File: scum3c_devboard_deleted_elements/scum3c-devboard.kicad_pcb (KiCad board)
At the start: 4 copper layers, 30 x 30 mm, 23 parts, among them J1 Conn_01x14, U8 scum3, U9AB1 MPU-9250

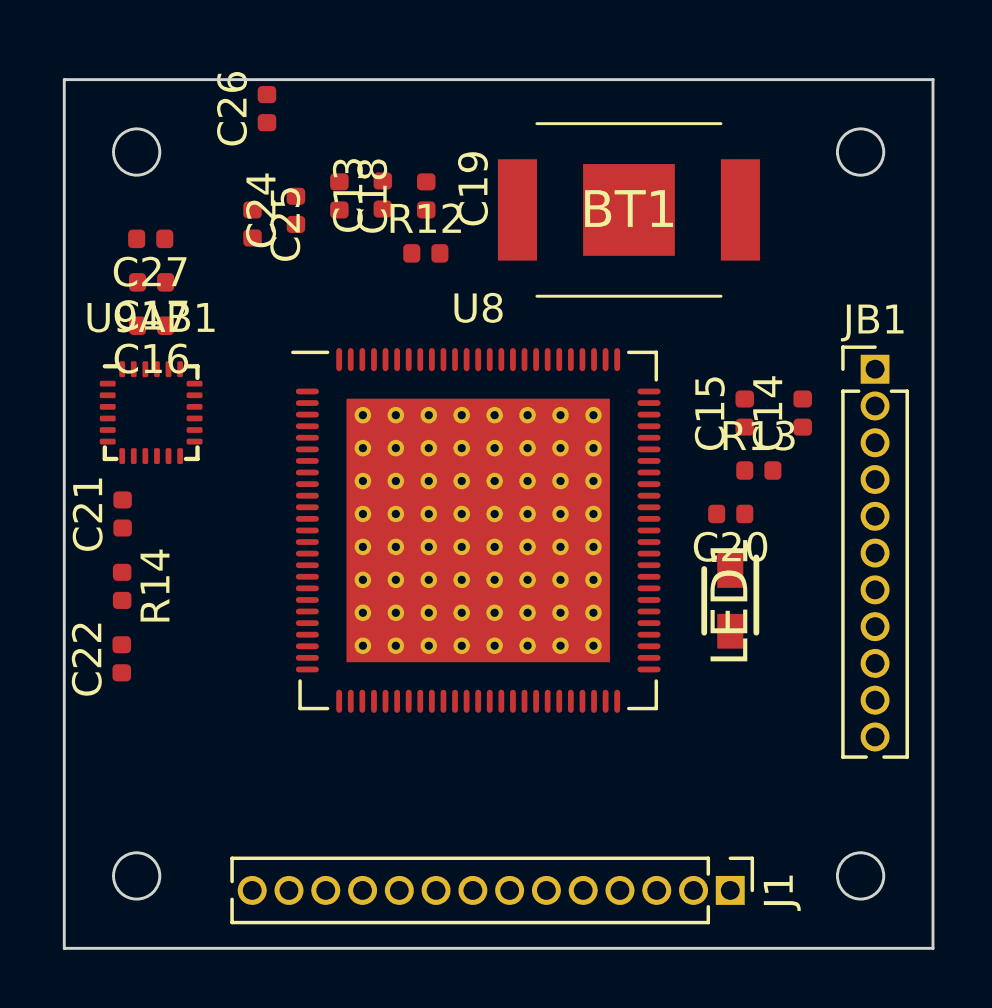
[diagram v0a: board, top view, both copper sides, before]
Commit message: Revert "added gpio8-10"
This reverts commit daf7284f57cd8196d10e3621e3573955ecb68719.
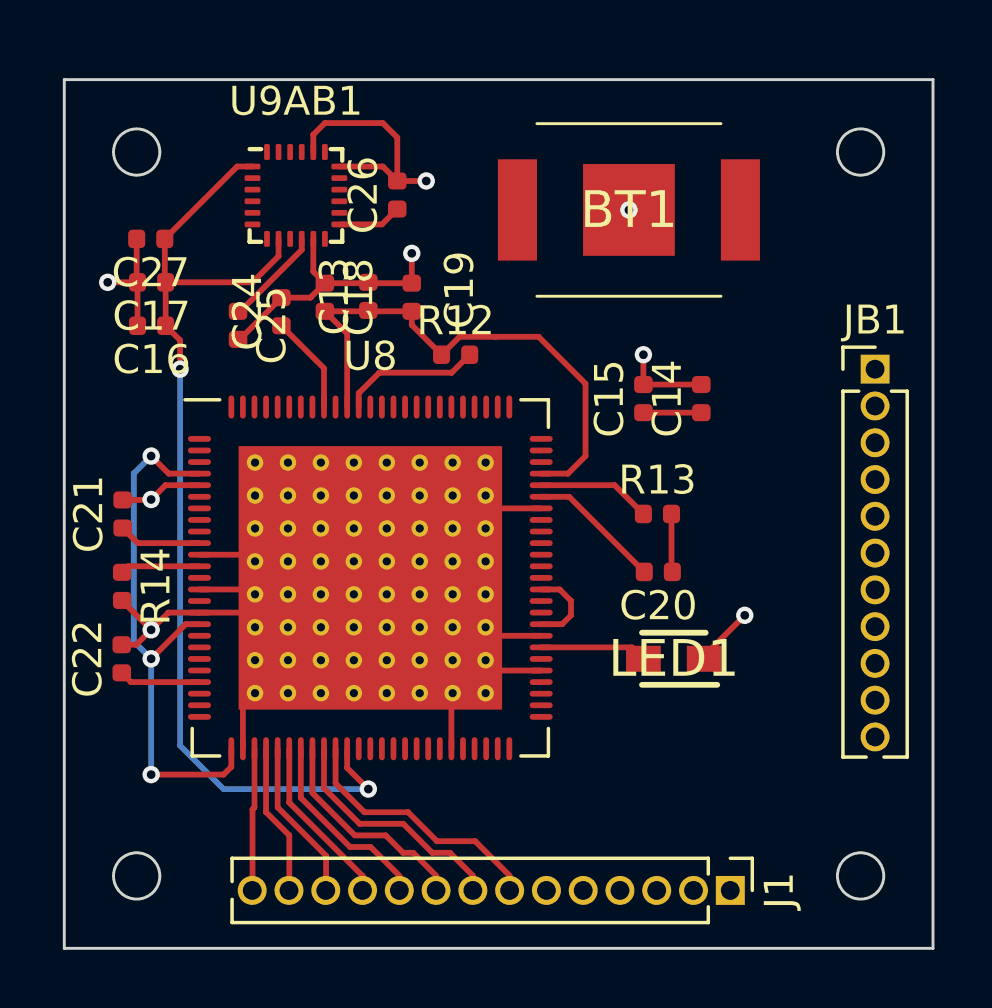
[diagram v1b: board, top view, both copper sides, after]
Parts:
- moved U9AB1 9.01 mm to (95.5, 81.5)
- moved C26 5.40 mm to (99.0, 81.5)
- moved U8 4.07 mm to (98.1, 94.7)
- moved R13 3.81 mm to (108.0, 92.5)
- moved R12 3.65 mm to (101.0, 87.0)
- moved C13 3.54 mm to (98.0, 85.0)
- moved C14 3.54 mm to (109.5, 88.5)
- moved C15 3.54 mm to (107.5, 88.5)
- moved C18 3.54 mm to (96.5, 85.0)
- moved C19 3.54 mm to (99.5, 85.0)
- moved C24 3.54 mm to (95.0, 85.5)
- moved C25 3.54 mm to (93.5, 86.0)
- moved C20 3.20 mm to (108.0, 94.5)
- moved LED1 2.79 mm to (108.5, 97.5), turned to 180 degrees
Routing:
- net GND: track 0.00 -> 53.1 mm, vias 0 -> 8
- net +VDDIO: track 0.00 -> 35.5 mm, vias 0 -> 2
- net +VBAT: track 0.00 -> 23.9 mm, vias 0 -> 3
- net +VDDD: track 0.00 -> 18.8 mm
- net /GPIO7: track 0.00 -> 8.54 mm
- net /GPIO6: track 0.00 -> 7.77 mm
- net /GPIO5: track 0.00 -> 7.00 mm
- net /GPIO4: track 0.00 -> 6.22 mm
- net /GPIO3: track 0.00 -> 5.45 mm
- net /GPIO2: track 0.00 -> 5.09 mm
- net Net-(R12-Pad2): track 0.00 -> 4.86 mm
- net /GPIO1: track 0.00 -> 4.73 mm
- net /scumsheet/AUX_LDO_OUTPUT: track 0.00 -> 4.64 mm
- net /GPIO0: track 0.00 -> 4.42 mm
- net Net-(R13-Pad1): track 0.00 -> 3.94 mm
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
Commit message: deleted tracks
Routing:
- net GND: track 53.1 -> 0.00 mm, vias 8 -> 0
- net +VDDIO: track 35.5 -> 0.00 mm, vias 2 -> 0
- net +VBAT: track 23.9 -> 0.00 mm, vias 3 -> 0
- net +VDDD: track 18.8 -> 0.00 mm
- net /GPIO7: track 8.54 -> 0.00 mm
- net /GPIO6: track 7.77 -> 0.00 mm
- net /GPIO5: track 7.00 -> 0.00 mm
- net /GPIO4: track 6.22 -> 0.00 mm
- net /GPIO3: track 5.45 -> 0.00 mm
- net /GPIO2: track 5.09 -> 0.00 mm
- net Net-(R12-Pad2): track 4.86 -> 0.00 mm
- net /GPIO1: track 4.73 -> 0.00 mm
- net /scumsheet/AUX_LDO_OUTPUT: track 4.64 -> 0.00 mm
- net /GPIO0: track 4.42 -> 0.00 mm
- net Net-(R13-Pad1): track 3.94 -> 0.00 mm
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
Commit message: placed components
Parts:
- moved C26 13.9 mm to (90.5, 92.5), turned to 180 degrees
- moved C15 8.60 mm to (114.5, 83.5), turned to 0 degrees
- moved C27 8.30 mm to (98.0, 79.5), turned to 90 degrees
- moved C16 7.88 mm to (95.0, 79.5), turned to 90 degrees
- moved C17 7.79 mm to (96.5, 79.5), turned to 90 degrees
- moved U9AB1 6.52 mm to (92.0, 87.0), turned to 270 degrees
- moved C14 5.83 mm to (114.5, 85.5), turned to 0 degrees
- moved R13 5.71 mm to (111.5, 88.0)
- moved C20 5.70 mm to (111.5, 90.0)
- moved C25 5.43 mm to (90.5, 90.5), turned to 0 degrees
- moved U8 4.61 mm to (102.4, 93.2)
- moved LED1 4.54 mm to (111.5, 94.0), turned to 270 degrees
- moved R12 3.65 mm to (100.0, 83.5)
- moved C24 3.23 mm to (93.0, 83.0)
- moved C13 2.50 mm to (96.5, 83.0)
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
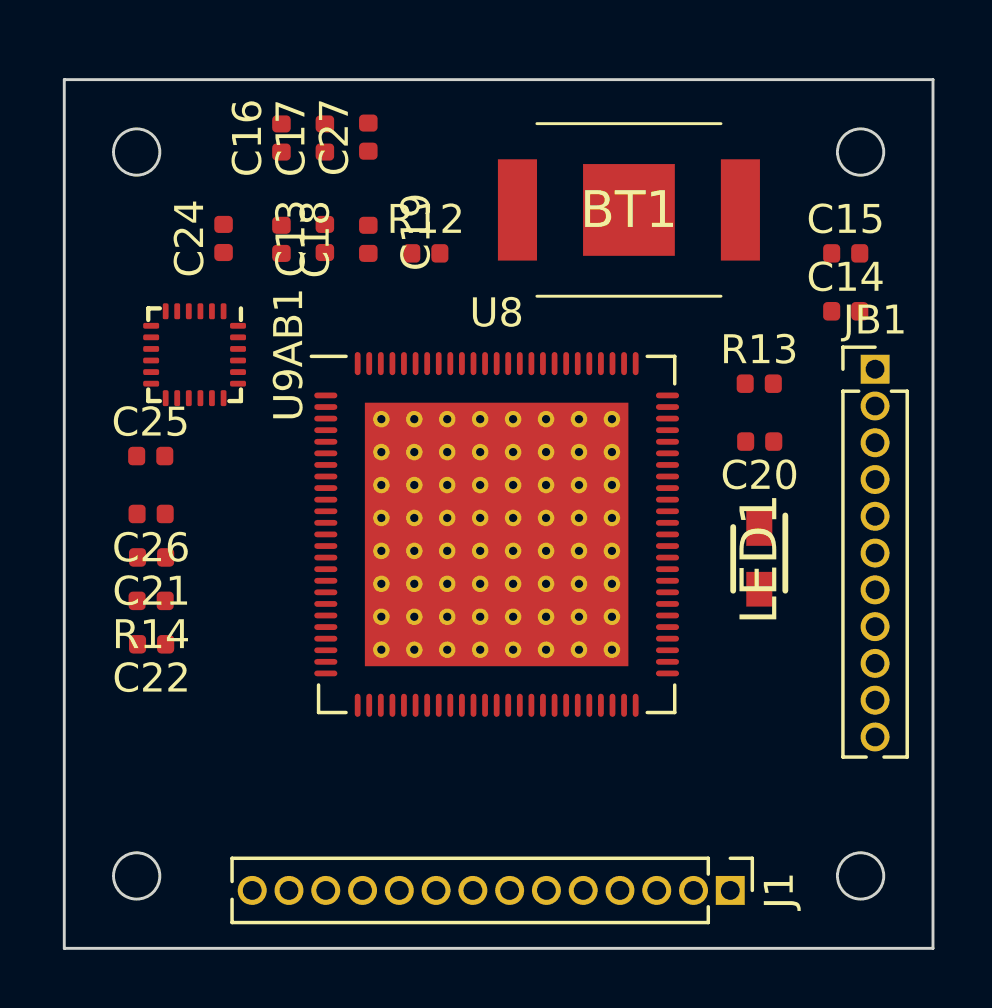
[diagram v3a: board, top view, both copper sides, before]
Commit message: placed gpio, adc, and 3wb tracks
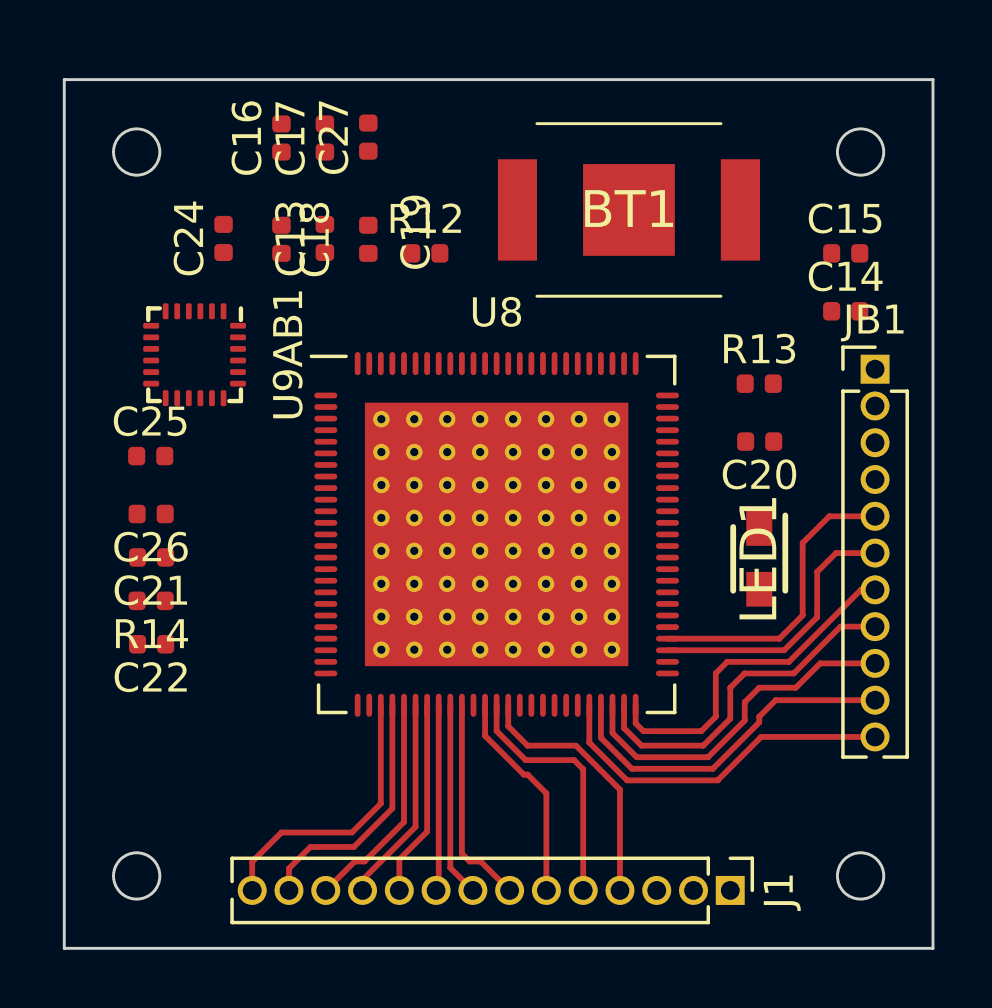
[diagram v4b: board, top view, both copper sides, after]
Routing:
- net /RsTx: track 0.00 -> 12.3 mm
- net /RsRx: track 0.00 -> 12.1 mm
- net /3WB_CLK: track 0.00 -> 12.1 mm
- net /3WB_ENB: track 0.00 -> 12.0 mm
- net /3WB_DATA: track 0.00 -> 11.9 mm
- net /SENSOR_EXT_IN: track 0.00 -> 10.4 mm
- net /GPIO0: track 0.00 -> 9.66 mm
- net /SENSOR_LDO_OUTPUT: track 0.00 -> 9.48 mm
- net /GPIO10: track 0.00 -> 8.97 mm
- net /GPIO1: track 0.00 -> 8.75 mm
- net /GPIO9: track 0.00 -> 8.61 mm
- net /GPIO2: track 0.00 -> 7.71 mm
- net /GPIO8: track 0.00 -> 7.35 mm
- net /GPIO7: track 0.00 -> 7.30 mm
- net /GPIO3: track 0.00 -> 7.15 mm
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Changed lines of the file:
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@@
     (thickness 1.6)
     (drawings 12)
-    (tracks 0)
+    (tracks 92)
     (zones 0)
     (modules 23)
@@
   (gr_line (start 87.5 107.5) (end 87.5 77.5) (layer Edge.Cuts) (width 0.1))
   (gr_line (start 117.5 107.5) (end 87.5 107.5) (layer Edge.Cuts) (width 0.1))
+  (segment (start 101.23125 99.10625) (end 101.23125 104.23125) (width 0.2) (layer F.Cu) (net 11))
+  (segment (start 101.23125 104.23125) (end 101.5 104.5) (width 0.2) (layer F.Cu) (net 11))
+  (segment (start 101.88 104.5) (end 102.88 105.5) (width 0.2) (layer F.Cu) (net 11))
+  (segment (start 101.5 104.5) (end 101.88 104.5) (width 0.2) (layer F.Cu) (net 11))
+  (segment (start 100.43125 105.40875) (end 100.34 105.5) (width 0.2) (layer F.Cu) (net 12))
+  (segment (start 100.43125 99.10625) (end 100.43125 105.40875) (width 0.2) (layer F.Cu) (net 12))
+  (segment (start 97.8 105.134301) (end 97.8 105.5) (width 0.2) (layer F.Cu) (net 13))
+  (segment (start 99.63125 103.303052) (end 97.8 105.134301) (width 0.2) (layer F.Cu) (net 13))
+  (segment (start 99.63125 99.10625) (end 99.63125 103.303052) (width 0.2) (layer F.Cu) (net 13))
+  (segment (start 98.83125 99.10625) (end 98.83125 102.66875) (width 0.2) (layer F.Cu) (net 14))
+  (segment (start 98.83125 102.66875) (end 97.5 104) (width 0.2) (layer F.Cu) (net 14))
+  (segment (start 97.5 104) (end 96 104) (width 0.2) (layer F.Cu) (net 14))
+  (segment (start 95.26 104.74) (end 95.26 105.5) (width 0.2) (layer F.Cu) (net 14))
+  (segment (start 96 104) (end 95.26 104.74) (width 0.2) (layer F.Cu) (net 14))
+  (segment (start 100.83125 104.72125) (end 101.61 105.5) (width 0.2) (layer F.Cu) (net 15))
+  (segment (start 100.83125 99.10625) (end 100.83125 104.72125) (width 0.2) (layer F.Cu) (net 15))
+  (segment (start 100.03125 99.10625) (end 100.03125 103.46875) (width 0.2) (layer F.Cu) (net 16))
+  (segment (start 99.07 104.43) (end 99.07 105.5) (width 0.2) (layer F.Cu) (net 16))
+  (segment (start 100.03125 103.46875) (end 99.07 104.43) (width 0.2) (layer F.Cu) (net 16))
+  (segment (start 99.23125 99.10625) (end 99.23125 103.137354) (width 0.2) (layer F.Cu) (net 17))
+  (segment (start 99.23125 103.137354) (end 97.868604 104.5) (width 0.2) (layer F.Cu) (net 17))
+  (segment (start 97.53 104.5) (end 96.53 105.5) (width 0.2) (layer F.Cu) (net 17))
+  (segment (start 97.868604 104.5) (end 97.53 104.5) (width 0.2) (layer F.Cu) (net 17))
+  (segment (start 98.43125 99.10625) (end 98.43125 102.503052) (width 0.2) (layer F.Cu) (net 18))
+  (segment (start 98.43125 102.503052) (end 97.434302 103.5) (width 0.2) (layer F.Cu) (net 18))
+  (segment (start 97.434302 103.5) (end 95 103.5) (width 0.2) (layer F.Cu) (net 18))
+  (segment (start 93.99 104.51) (end 93.99 105.5) (width 0.2) (layer F.Cu) (net 18))
+  (segment (start 95 103.5) (end 93.99 104.51) (width 0.2) (layer F.Cu) (net 18))
+  (segment (start 115.011396 95.12) (end 115.5 95.12) (width 0.2) (layer F.Cu) (net 22))
+  (segment (start 112.525137 97.60626) (end 115.011396 95.12) (width 0.2) (layer F.Cu) (net 22))
+  (segment (start 110.39374 97.60626) (end 112.525137 97.60626) (width 0.2) (layer F.Cu) (net 22))
+  (segment (start 110 98) (end 110.39374 97.60626) (width 0.2) (layer F.Cu) (net 22))
+  (segment (start 107.5 100) (end 109.5 100) (width 0.2) (layer F.Cu) (net 22))
+  (segment (start 107.23125 99.10625) (end 107.23125 99.73125) (width 0.2) (layer F.Cu) (net 22))
+  (segment (start 109.5 100) (end 110 99.5) (width 0.2) (layer F.Cu) (net 22))
+  (segment (start 107.23125 99.73125) (end 107.5 100) (width 0.2) (layer F.Cu) (net 22))
+  (segment (start 110 99.5) (end 110 98) (width 0.2) (layer F.Cu) (net 22))
+  (segment (start 106.83125 99.896948) (end 107.434302 100.5) (width 0.2) (layer F.Cu) (net 23))
+  (segment (start 106.83125 99.10625) (end 106.83125 99.896948) (width 0.2) (layer F.Cu) (net 23))
+  (segment (start 109.565698 100.5) (end 110.5 99.565698) (width 0.2) (layer F.Cu) (net 23))
+  (segment (start 107.434302 100.5) (end 109.565698 100.5) (width 0.2) (layer F.Cu) (net 23))
+  (segment (start 110.5 98.5) (end 110.99373 98.00627) (width 0.2) (layer F.Cu) (net 23))
+  (segment (start 110.5 99.565698) (end 110.5 98.5) (width 0.2) (layer F.Cu) (net 23))
+  (segment (start 114.307096 96.39) (end 115.5 96.39) (width 0.2) (layer F.Cu) (net 23))
+  (segment (start 112.690826 98.00627) (end 114.307096 96.39) (width 0.2) (layer F.Cu) (net 23))
+  (segment (start 110.99373 98.00627) (end 112.690826 98.00627) (width 0.2) (layer F.Cu) (net 23))
+  (segment (start 107.268613 100.90001) (end 109.731386 100.90001) (width 0.2) (layer F.Cu) (net 24))
+  (segment (start 106.43125 99.10625) (end 106.43125 100.062646) (width 0.2) (layer F.Cu) (net 24))
+  (segment (start 106.43125 100.062646) (end 107.268613 100.90001) (width 0.2) (layer F.Cu) (net 24))
+  (segment (start 109.731386 100.90001) (end 111 99.631396) (width 0.2) (layer F.Cu) (net 24))
+  (segment (start 111 99.631396) (end 111 99) (width 0.2) (layer F.Cu) (net 24))
+  (segment (start 111 99) (end 111.5 98.5) (width 0.2) (layer F.Cu) (net 24))
+  (segment (start 111.5 98.5) (end 112.762794 98.5) (width 0.2) (layer F.Cu) (net 24))
+  (segment (start 113.602794 97.66) (end 115.5 97.66) (width 0.2) (layer F.Cu) (net 24))
+  (segment (start 112.762794 98.5) (end 113.602794 97.66) (width 0.2) (layer F.Cu) (net 24))
+  (segment (start 111.562793 100.2) (end 115.5 100.2) (width 0.2) (layer F.Cu) (net 25))
+  (segment (start 110.062764 101.70003) (end 111.562793 100.2) (width 0.2) (layer F.Cu) (net 25))
+  (segment (start 106.937235 101.70003) (end 110.062764 101.70003) (width 0.2) (layer F.Cu) (net 25))
+  (segment (start 105.63125 99.10625) (end 105.63125 100.394044) (width 0.2) (layer F.Cu) (net 25))
+  (segment (start 105.63125 100.394044) (end 106.937235 101.70003) (width 0.2) (layer F.Cu) (net 25))
+  (segment (start 106.03125 100.228345) (end 107.102924 101.30002) (width 0.2) (layer F.Cu) (net 26))
+  (segment (start 106.03125 99.10625) (end 106.03125 100.228345) (width 0.2) (layer F.Cu) (net 26))
+  (segment (start 109.897075 101.30002) (end 111.5 99.697095) (width 0.2) (layer F.Cu) (net 26))
+  (segment (start 107.102924 101.30002) (end 109.897075 101.30002) (width 0.2) (layer F.Cu) (net 26))
+  (segment (start 111.5 99.697095) (end 111.5 99.5) (width 0.2) (layer F.Cu) (net 26))
+  (segment (start 112.07 98.93) (end 115.5 98.93) (width 0.2) (layer F.Cu) (net 26))
+  (segment (start 111.5 99.5) (end 112.07 98.93) (width 0.2) (layer F.Cu) (net 26))
+  (segment (start 112.359448 97.20625) (end 113.5 96.065698) (width 0.2) (layer F.Cu) (net 28))
+  (segment (start 108.33125 97.20625) (end 112.359448 97.20625) (width 0.2) (layer F.Cu) (net 28))
+  (segment (start 113.5 96.065698) (end 113.5 94.5) (width 0.2) (layer F.Cu) (net 28))
+  (segment (start 114.15 93.85) (end 115.5 93.85) (width 0.2) (layer F.Cu) (net 28))
+  (segment (start 113.5 94.5) (end 114.15 93.85) (width 0.2) (layer F.Cu) (net 28))
+  (segment (start 108.33125 96.80625) (end 112.19375 96.80625) (width 0.2) (layer F.Cu) (net 29))
+  (segment (start 112.19375 96.80625) (end 113 96) (width 0.2) (layer F.Cu) (net 29))
+  (segment (start 113 96) (end 113 93.5) (width 0.2) (layer F.Cu) (net 29))
+  (segment (start 113.92 92.58) (end 115.5 92.58) (width 0.2) (layer F.Cu) (net 29))
+  (segment (start 113 93.5) (end 113.92 92.58) (width 0.2) (layer F.Cu) (net 29))
+  (segment (start 103.5 100.5) (end 105.171508 100.500001) (width 0.2) (layer F.Cu) (net 30))
+  (segment (start 102.83125 99.10625) (end 102.83125 99.83125) (width 0.2) (layer F.Cu) (net 30))
+  (segment (start 106.69 102.018493) (end 106.69 105.5) (width 0.2) (layer F.Cu) (net 30))
+  (segment (start 105.171508 100.500001) (end 106.69 102.018493) (width 0.2) (layer F.Cu) (net 30))
+  (segment (start 102.83125 99.83125) (end 103.5 100.5) (width 0.2) (layer F.Cu) (net 30))
+  (segment (start 105.105809 101) (end 105.42 101.314191) (width 0.2) (layer F.Cu) (net 31))
+  (segment (start 105.42 101.314191) (end 105.42 105.5) (width 0.2) (layer F.Cu) (net 31))
+  (segment (start 103.434302 101) (end 105.105809 101) (width 0.2) (layer F.Cu) (net 31))
+  (segment (start 102.43125 99.10625) (end 102.43125 99.996948) (width 0.2) (layer F.Cu) (net 31))
+  (segment (start 102.43125 99.996948) (end 103.434302 101) (width 0.2) (layer F.Cu) (net 31))
+  (segment (start 104.15 102.15) (end 104.15 105.5) (width 0.2) (layer F.Cu) (net 32))
+  (segment (start 103.5 101.5) (end 104.15 102.15) (width 0.2) (layer F.Cu) (net 32))
+  (segment (start 103.368604 101.5) (end 103.5 101.5) (width 0.2) (layer F.Cu) (net 32))
+  (segment (start 102.03125 99.10625) (end 102.03125 100.162646) (width 0.2) (layer F.Cu) (net 32))
+  (segment (start 102.03125 100.162646) (end 103.368604 101.5) (width 0.2) (layer F.Cu) (net 32))
   (zone (net 2) (net_name GND) (layer In1.Cu) (hatch edge 0.508)
     (connect_pads yes (clearance 0.508))
